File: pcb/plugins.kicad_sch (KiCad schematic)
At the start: 6 parts

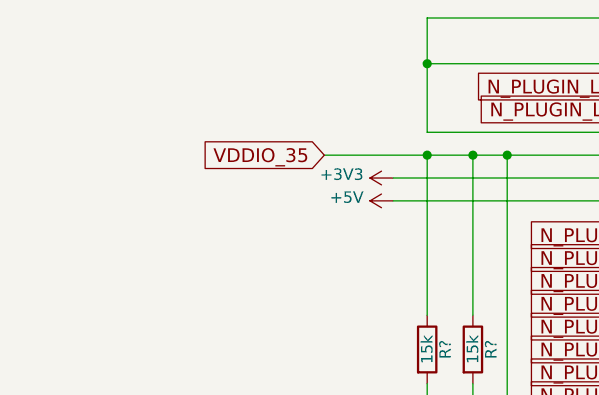
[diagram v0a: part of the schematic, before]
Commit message: Change Plans: two image sensors
* Redo power management
* Add level shifters
* Intention to use both image sensors on the same board
* Add Pmod & LEDs
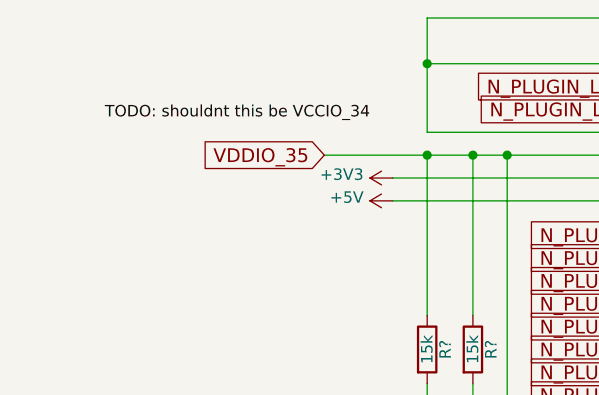
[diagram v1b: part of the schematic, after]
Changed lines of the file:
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@@
     (stroke (width 0) (type solid) (color 0 0 0 0))
+  )
+  (label "TODO: shouldnt this be VCCIO_34" (at 62.23 54.61 180)
+    (effects (font (size 1.27 1.27)) (justify right bottom))
   )
   (global_label "VDDIO_35" (shape input) (at 57.15 58.42 180)    (property "Intersheet References" "${INTERSHEET_REFS}" (id 0) (at -243.84 -151.13 0)

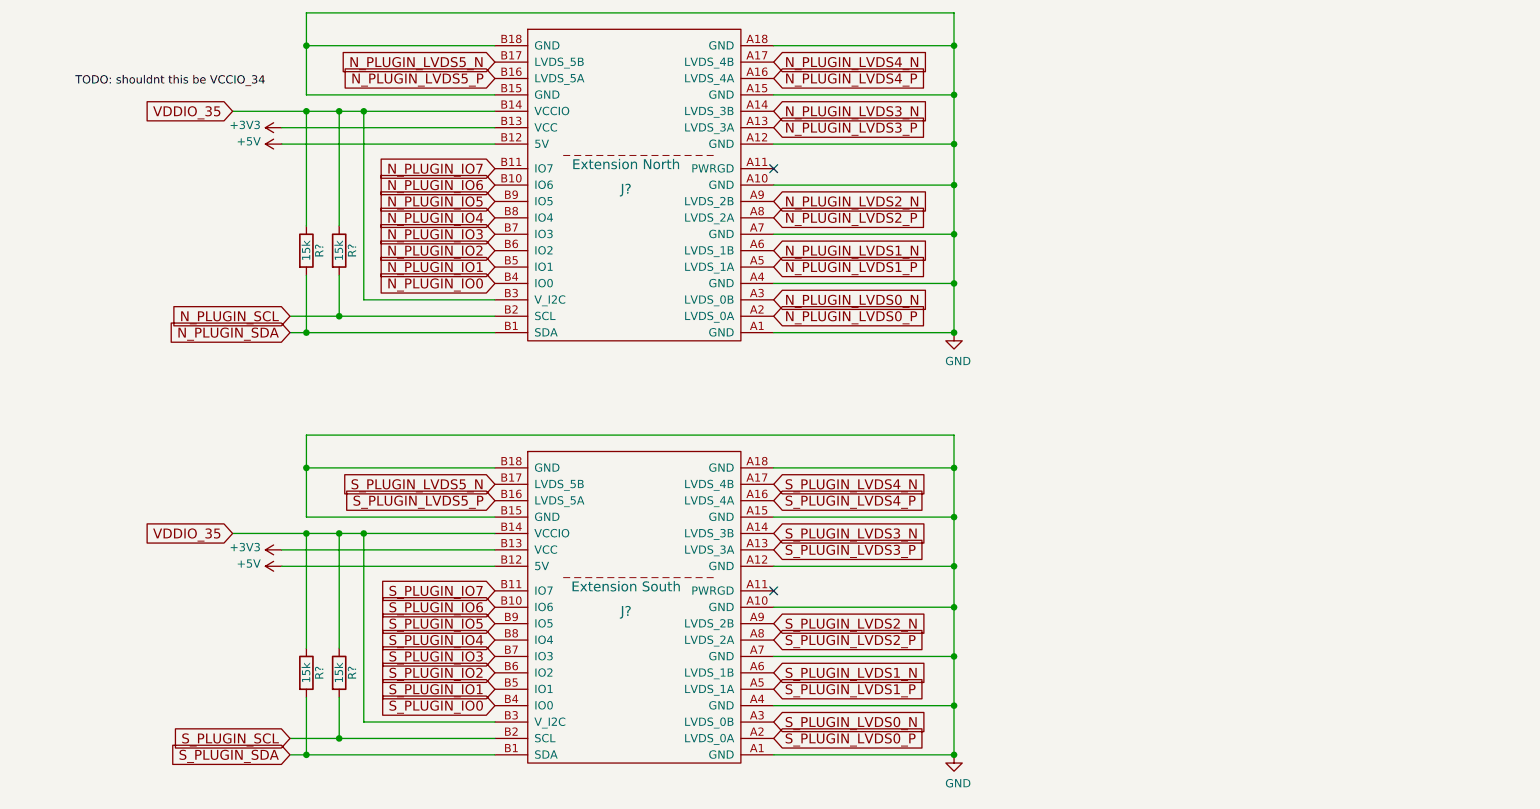
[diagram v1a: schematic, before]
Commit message: add i2c addresses
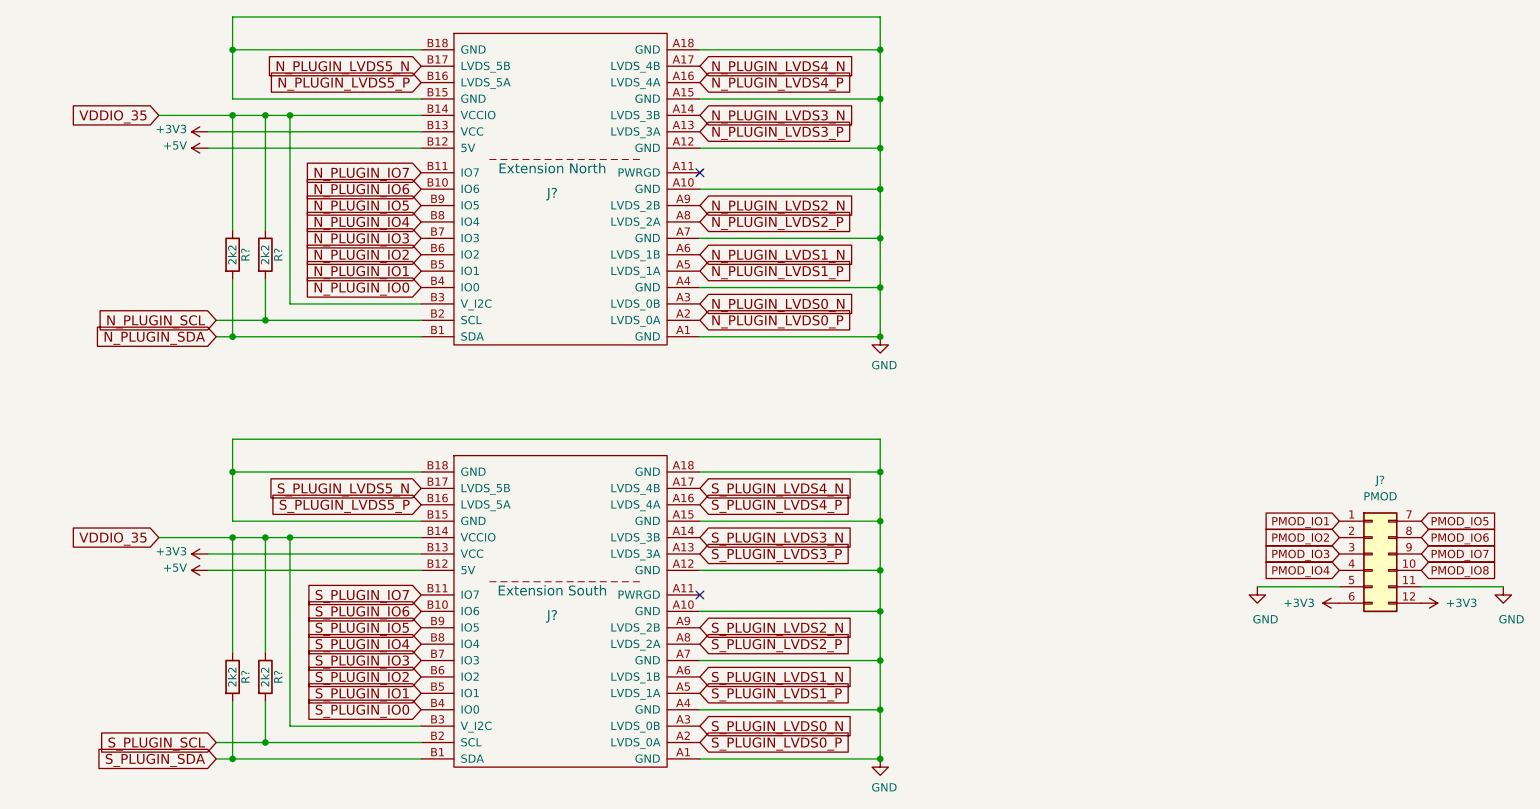
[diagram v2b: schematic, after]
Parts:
- added J?: PMOD, symbol Connector_Generic:Conn_02x06_Top_Bottom
- R? (x4): value 15k -> 2k2
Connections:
- net +3V3: now also J?.12 (Pin_12), J?.6 (Pin_6)
- net GND: now also J?.11 (Pin_11), J?.5 (Pin_5)
- new net PMOD_IO1: J?.1 (Pin_1)
- new net PMOD_IO2: J?.2 (Pin_2)
- new net PMOD_IO3: J?.3 (Pin_3)
- new net PMOD_IO4: J?.4 (Pin_4)
- new net PMOD_IO5: J?.7 (Pin_7)
- new net PMOD_IO6: J?.8 (Pin_8)
- new net PMOD_IO7: J?.9 (Pin_9)
- new net PMOD_IO8: J?.10 (Pin_10)
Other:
- moved on the sheet: J?, R?
